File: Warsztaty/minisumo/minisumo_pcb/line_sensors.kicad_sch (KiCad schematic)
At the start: 9 parts, among them U1 ITR8307-S17-TR8, U3 ITR8307-S17-TR8, U6 ITR8307-S17-TR8

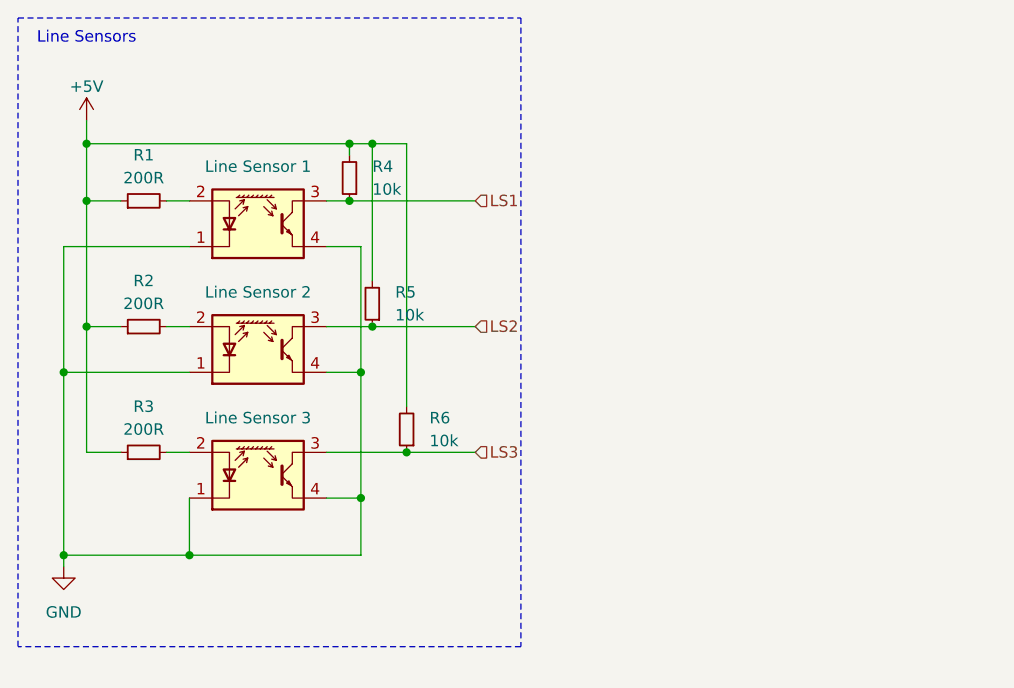
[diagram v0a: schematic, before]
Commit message: laczenie hierarchiczne schematu
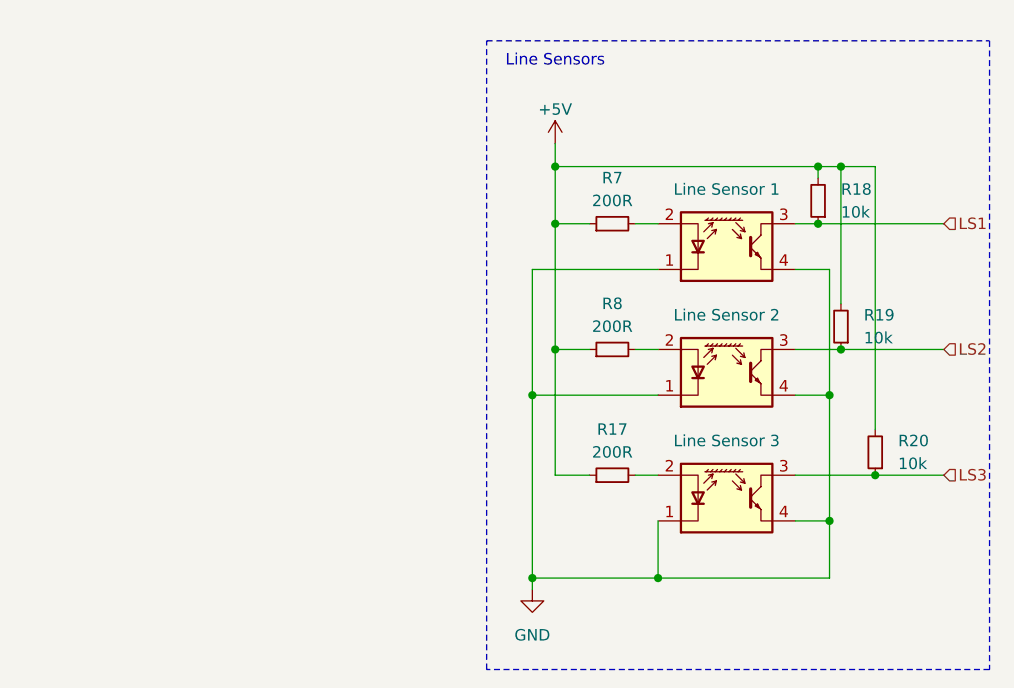
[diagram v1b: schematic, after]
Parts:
- removed R1, R2, R3: 200R, symbol Device:R_Small
- removed R4, R5, R6: 10k, symbol Device:R_Small
- removed U1, U3, U6: ITR8307-S17-TR8, OptoDevice:Everlight_ITR1201SR10AR, symbol Sensor_Proximity:ITR8307-S17-TR8
- added R17, R7, R8: 200R, symbol Device:R_Small
- added R18, R19, R20: 10k, symbol Device:R_Small
- added U10, U11, U8: ITR8307-S17-TR8, OptoDevice:Everlight_ITR1201SR10AR, symbol Sensor_Proximity:ITR8307-S17-TR8
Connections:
- net +5V: now also R17.1, R18.2, R19.2, R20.2, R7.1, R8.1
- net GND: now also U10.1 (K), U10.4, U11.1 (K), U11.4, U8.1 (K), U8.4
- net LS1: now also R18.1, U8.3
- net LS2: now also R19.1, U10.3
- net LS3: now also R20.1, U11.3
- new net: R17.2, U11.2 (A)
- new net: R8.2, U10.2 (A)
- new net: R7.2, U8.2 (A)

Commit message: chyba gotowy schemat
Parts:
- R17, R18, R19, R20, R7, R8: footprint (none) -> Resistor_SMD:R_0805_2012Metric_Pad1.20x1.40mm_HandSolder
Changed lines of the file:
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@@
 			)
 		)
-		(property "Footprint" ""
+		(property "Footprint" "Resistor_SMD:R_0805_2012Metric_Pad1.20x1.40mm_HandSolder"
 			(at 105.41 49.53 0)
 			(effects
@@
 			)
 		)
-		(property "Footprint" ""
+		(property "Footprint" "Resistor_SMD:R_0805_2012Metric_Pad1.20x1.40mm_HandSolder"
 			(at 80.01 66.04 0)
 			(effects
@@
 			)
 		)
-		(property "Footprint" ""
+		(property "Footprint" "Resistor_SMD:R_0805_2012Metric_Pad1.20x1.40mm_HandSolder"
 			(at 102.87 35.56 0)
 			(effects
@@
 			)
 		)
-		(property "Footprint" ""
+		(property "Footprint" "Resistor_SMD:R_0805_2012Metric_Pad1.20x1.40mm_HandSolder"
 			(at 80.01 38.1 0)
 			(effects
@@
 			)
 		)
-		(property "Footprint" ""
+		(property "Footprint" "Resistor_SMD:R_0805_2012Metric_Pad1.20x1.40mm_HandSolder"
 			(at 80.01 52.07 0)
 			(effects
@@
 			)
 		)
-		(property "Footprint" ""
+		(property "Footprint" "Resistor_SMD:R_0805_2012Metric_Pad1.20x1.40mm_HandSolder"
 			(at 109.22 63.5 0)
 			(effects

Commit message: chyba gotowy schemat
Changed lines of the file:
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@@
 	)
 	(hierarchical_label "LS1"
-		(shape input)
+		(shape output)
 		(at 116.84 38.1 0)
 		(fields_autoplaced yes)
@@
 	)
 	(hierarchical_label "LS2"
-		(shape input)
+		(shape output)
 		(at 116.84 52.07 0)
 		(fields_autoplaced yes)
@@
 	)
 	(hierarchical_label "LS3"
-		(shape input)
+		(shape output)
 		(at 116.84 66.04 0)
 		(fields_autoplaced yes)

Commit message: stan przed usunięciem jednego czujnika lini
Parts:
- R17, R18, R19, R20, R7, R8: footprint Resistor_SMD:R_0805_2012Metric_Pad1.20x1.40mm_HandSolder -> Resistor_SMD:R_0805_2012Metric
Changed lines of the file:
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@@
 			)
 		)
-		(property "Footprint" "Resistor_SMD:R_0805_2012Metric_Pad1.20x1.40mm_HandSolder"
+		(property "Footprint" "Resistor_SMD:R_0805_2012Metric"
 			(at 105.41 49.53 0)
 			(effects
@@
 			)
 		)
-		(property "Footprint" "Resistor_SMD:R_0805_2012Metric_Pad1.20x1.40mm_HandSolder"
+		(property "Footprint" "Resistor_SMD:R_0805_2012Metric"
 			(at 80.01 66.04 0)
 			(effects
@@
 			)
 		)
-		(property "Footprint" "Resistor_SMD:R_0805_2012Metric_Pad1.20x1.40mm_HandSolder"
+		(property "Footprint" "Resistor_SMD:R_0805_2012Metric"
 			(at 102.87 35.56 0)
 			(effects
@@
 			)
 		)
-		(property "Footprint" "Resistor_SMD:R_0805_2012Metric_Pad1.20x1.40mm_HandSolder"
+		(property "Footprint" "Resistor_SMD:R_0805_2012Metric"
 			(at 80.01 38.1 0)
 			(effects
@@
 			)
 		)
-		(property "Footprint" "Resistor_SMD:R_0805_2012Metric_Pad1.20x1.40mm_HandSolder"
+		(property "Footprint" "Resistor_SMD:R_0805_2012Metric"
 			(at 80.01 52.07 0)
 			(effects
@@
 			)
 		)
-		(property "Footprint" "Resistor_SMD:R_0805_2012Metric_Pad1.20x1.40mm_HandSolder"
+		(property "Footprint" "Resistor_SMD:R_0805_2012Metric"
 			(at 109.22 63.5 0)
 			(effects

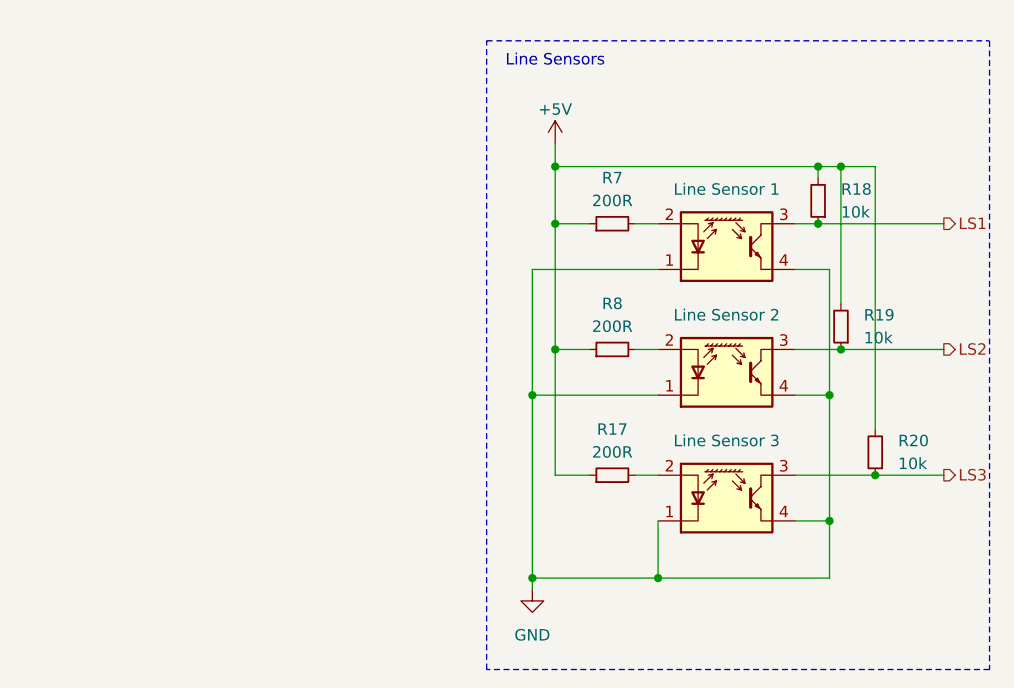
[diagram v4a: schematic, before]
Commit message: Wstępny wyglad robota i płytki
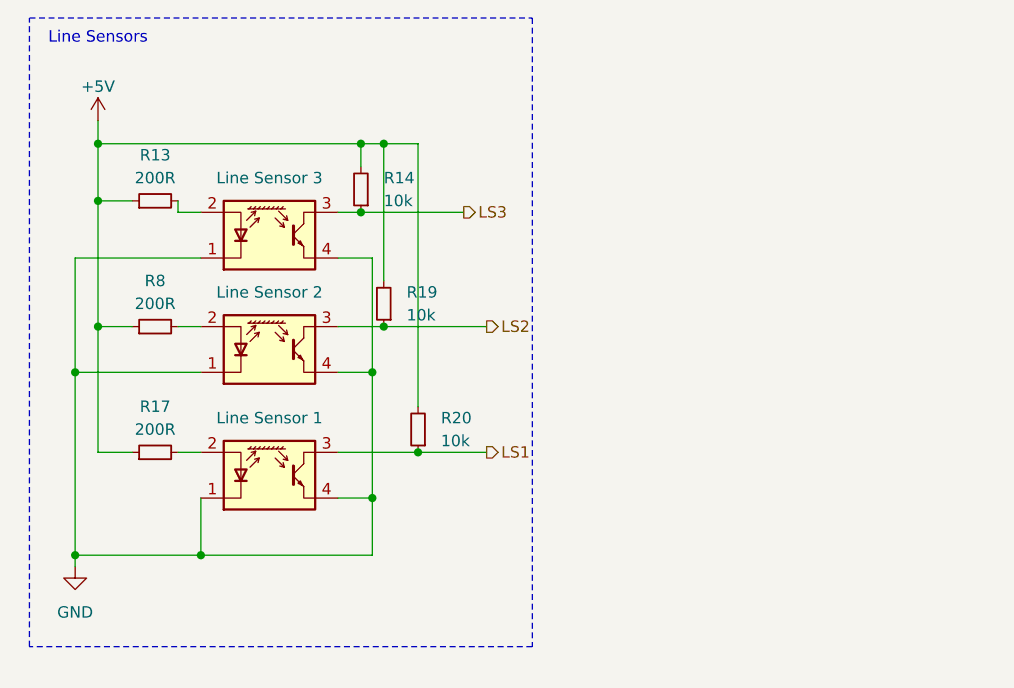
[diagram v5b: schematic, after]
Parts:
- removed R18: 10k, Resistor_SMD:R_0805_2012Metric, symbol Device:R_Small
- removed R7: 200R, Resistor_SMD:R_0805_2012Metric, symbol Device:R_Small
- removed U8: ITR8307-S17-TR8, OptoDevice:Everlight_ITR1201SR10AR, symbol Sensor_Proximity:ITR8307-S17-TR8
- added R13: 200R, Resistor_SMD:R_0805_2012Metric, symbol Device:R_Small
- added R14: 10k, Resistor_SMD:R_0805_2012Metric, symbol Device:R_Small
- added U3: ITR8307-S17-TR8, OptoDevice:Everlight_ITR1201SR10AR, symbol Sensor_Proximity:ITR8307-S17-TR8
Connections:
- net +5V: now also R13.1, R14.2
- net GND: now also U3.1 (K), U3.4
- net LS1: now also R20.1, U11.3
- net LS3: now also R14.1, U3.3; no longer R20.1, U11.3
- new net: R13.2, U3.2 (A)
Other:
- moved on the sheet: R17, R19, R20, R8

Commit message: koncowy projekt plytki i chyba model tez
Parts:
- renumbered U11 to LS1, U10 to LS2, U3 to LS3
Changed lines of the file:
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@@
 		(on_board yes)
 		(dnp no)
-		(property "Reference" "U11"
+		(property "Reference" "LS1"
 			(at 41.91 57.15 0)
 			(effects
@@
 			(project "minisumo_pcb"
 				(path "/7b99a4ad-c15f-48f5-acdf-b2b295c8ee3b/58eb88b1-485d-48c7-98a0-3f1f875455f5"
-					(reference "U11")
+					(reference "LS1")
 					(unit 1)
 				)
@@
 		(on_board yes)
 		(dnp no)
-		(property "Reference" "U10"
+		(property "Reference" "LS2"
 			(at 41.91 43.18 0)
 			(effects
@@
 			(project "minisumo_pcb"
 				(path "/7b99a4ad-c15f-48f5-acdf-b2b295c8ee3b/58eb88b1-485d-48c7-98a0-3f1f875455f5"
-					(reference "U10")
+					(reference "LS2")
 					(unit 1)
 				)
@@
 		(on_board yes)
 		(dnp no)
-		(property "Reference" "U3"
+		(property "Reference" "LS3"
 			(at 41.91 30.48 0)
 			(effects
@@
 			(project "minisumo_pcb"
 				(path "/7b99a4ad-c15f-48f5-acdf-b2b295c8ee3b/58eb88b1-485d-48c7-98a0-3f1f875455f5"
-					(reference "U3")
+					(reference "LS3")
 					(unit 1)
 				)
